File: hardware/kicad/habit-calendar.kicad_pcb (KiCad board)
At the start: 2 copper layers, 96 x 100 mm, 94 parts, among them J1 Conn_01x01, J10 Conn_01x01, J11 Conn_01x01, J12 Conn_01x01, J13 Conn_01x01, J14 Conn_01x01, J15 Conn_01x01, J16 Conn_01x01, J17 Conn_01x01, J18 Conn_01x01, J19 Conn_01x01, J2 Conn_01x01, J20 Conn_01x01, J21 Conn_01x01, J22 Conn_01x01, J23 Conn_01x01, J24 Conn_01x01, J25 Conn_01x01, J26 Conn_01x01, J27 Conn_01x01, J29 Conn_01x01, J30 Conn_01x01, J31 Conn_01x01, J4 Conn_01x10, J5 Conn_01x10, J6 Conn_01x01, J7 Conn_01x01, J8 Conn_01x01, J9 Conn_01x01, SW1 TS-1187A-B-A-B, SW10 TS-1187A-B-A-B, SW11 TS-1187A-B-A-B, SW12 TS-1187A-B-A-B, SW2 TS-1187A-B-A-B, SW3 TS-1187A-B-A-B, SW4 TS-1187A-B-A-B, SW5 TS-1187A-B-A-B, SW6 TS-1187A-B-A-B, SW7 TS-1187A-B-A-B, SW8 TS-1187A-B-A-B, SW9 TS-1187A-B-A-B, U1 PY32F002AF15P6TU

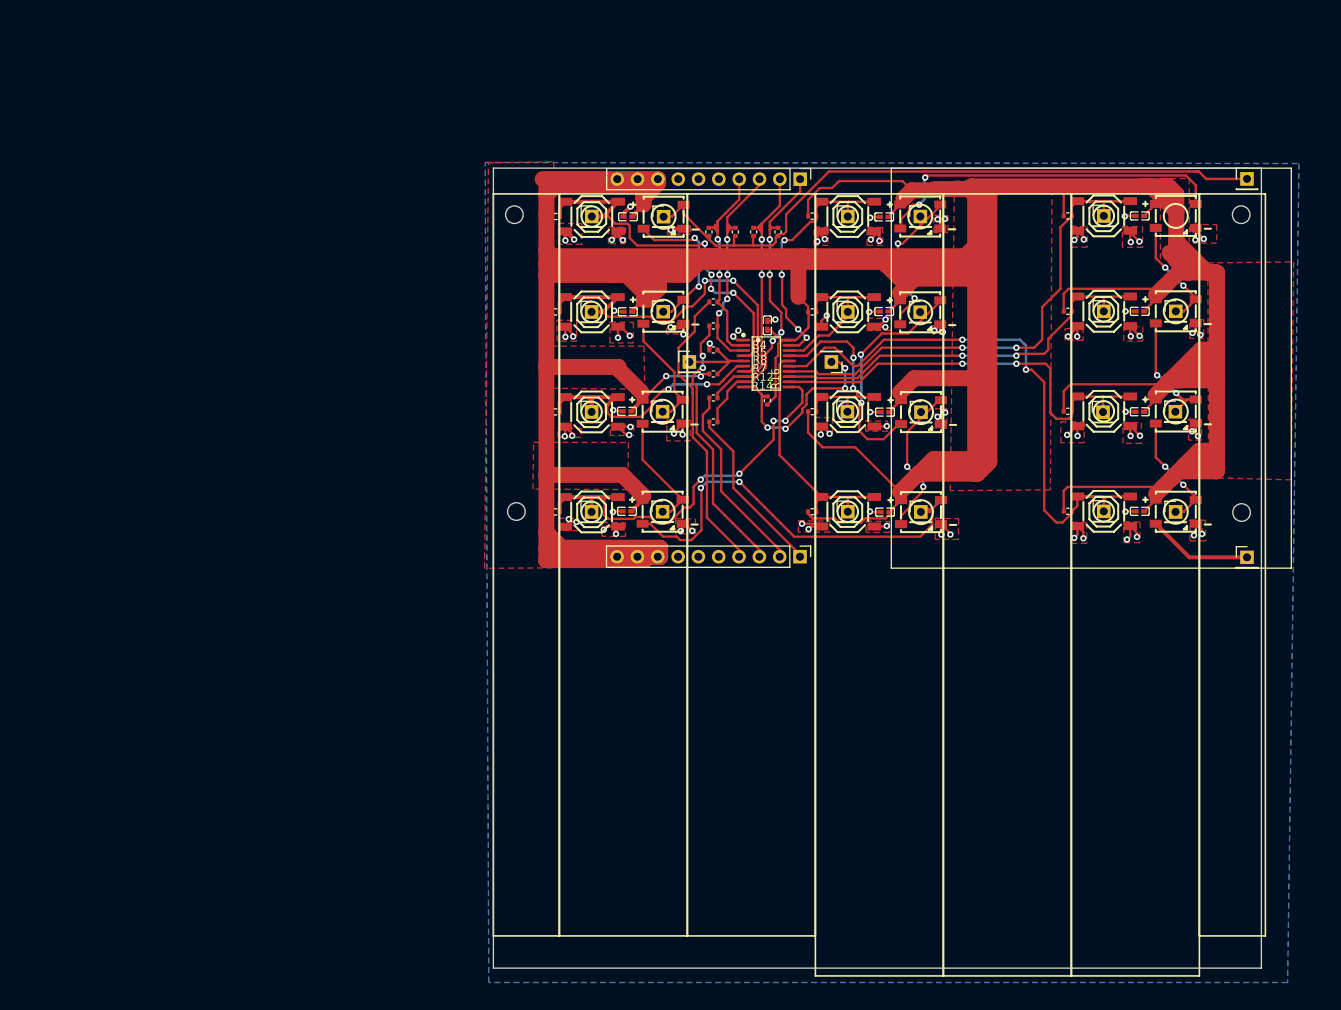
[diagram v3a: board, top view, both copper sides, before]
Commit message: Moved to a new heirarchical sheet. Instantiated two. Some PCB tweeks. Added Logo. Now going to use the replicate plugin to make another copy.
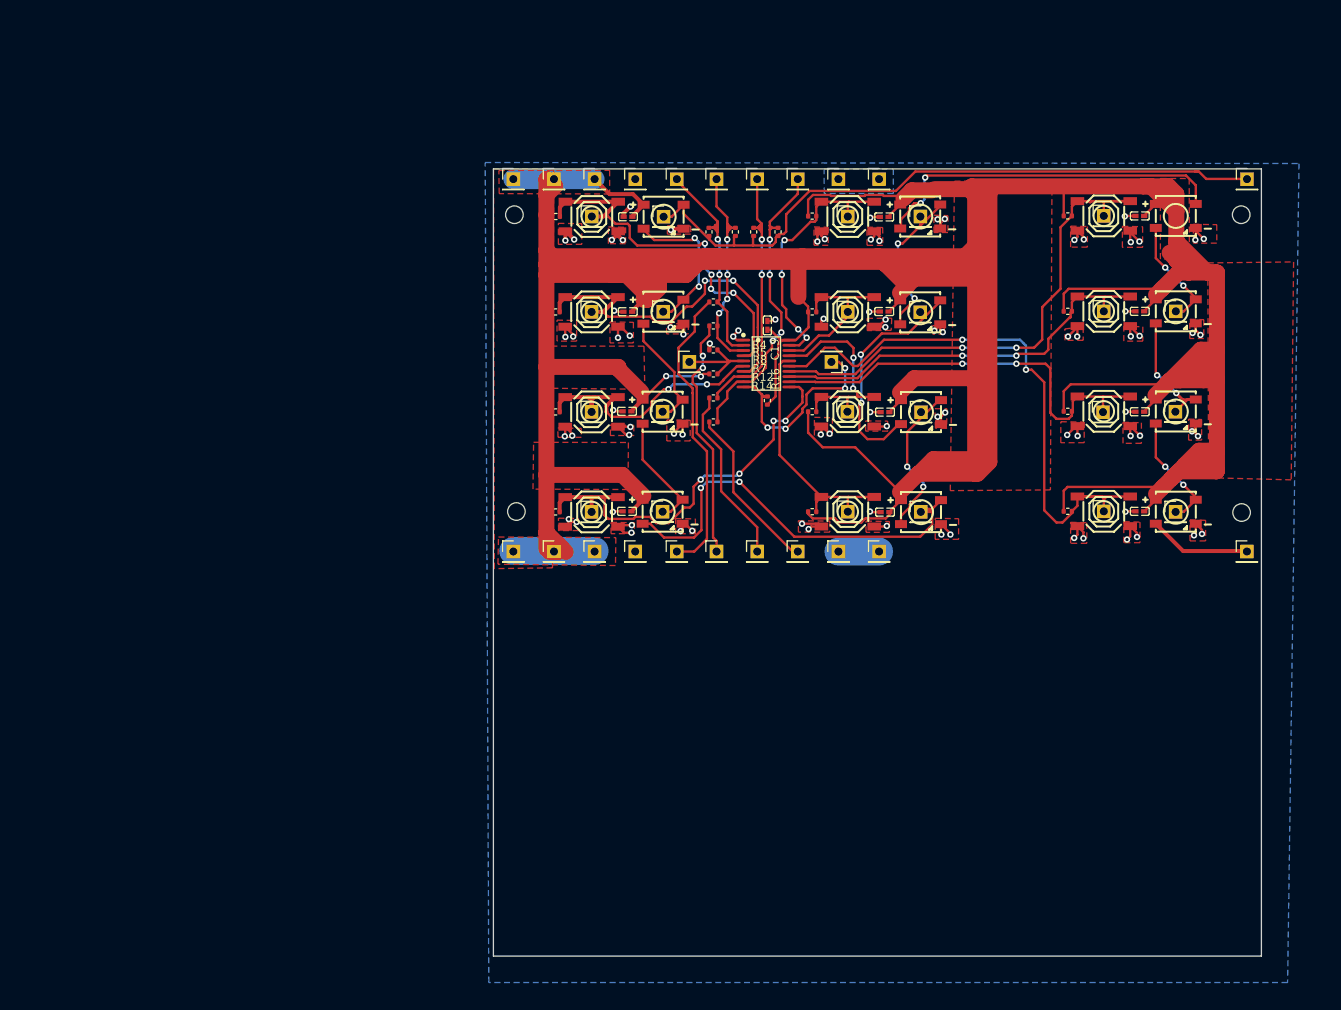
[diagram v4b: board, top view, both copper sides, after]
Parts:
- added G***: LOGO, LOGO, B.Cu at (197.8, 45.7)
- added J51: Conn_01x01, Connector_PinHeader_2.54mm:PinHeader_1x01_P2.54mm_Vertical, F.Cu at (125.2, 40.9)
- added J60: Conn_01x01, Connector_PinHeader_2.54mm:PinHeader_1x01_P2.54mm_Vertical, F.Cu at (130.2, 40.9)
- added J63: Conn_01x01, Connector_PinHeader_2.54mm:PinHeader_1x01_P2.54mm_Vertical, F.Cu at (160.7, 40.9)
- added J64: Conn_01x01, Connector_PinHeader_2.54mm:PinHeader_1x01_P2.54mm_Vertical, F.Cu at (155.6, 40.9)
- added J65: Conn_01x01, Connector_PinHeader_2.54mm:PinHeader_1x01_P2.54mm_Vertical, F.Cu at (135.4, 40.9)
- added J66: Conn_01x01, Connector_PinHeader_2.54mm:PinHeader_1x01_P2.54mm_Vertical, F.Cu at (140.4, 40.9)
- added J67: Conn_01x01, Connector_PinHeader_2.54mm:PinHeader_1x01_P2.54mm_Vertical, F.Cu at (145.5, 40.9)
- added J68: Conn_01x01, Connector_PinHeader_2.54mm:PinHeader_1x01_P2.54mm_Vertical, F.Cu at (150.6, 40.9)
- added J69: Conn_01x01, Connector_PinHeader_2.54mm:PinHeader_1x01_P2.54mm_Vertical, F.Cu at (115.0, 87.5)
- added J70: Conn_01x01, Connector_PinHeader_2.54mm:PinHeader_1x01_P2.54mm_Vertical, F.Cu at (120.1, 87.5)
- added J71: Conn_01x01, Connector_PinHeader_2.54mm:PinHeader_1x01_P2.54mm_Vertical, F.Cu at (125.2, 87.5)
- added J72: Conn_01x01, Connector_PinHeader_2.54mm:PinHeader_1x01_P2.54mm_Vertical, F.Cu at (130.2, 87.5)
- added J73: Conn_01x01, Connector_PinHeader_2.54mm:PinHeader_1x01_P2.54mm_Vertical, F.Cu at (155.6, 87.5)
- added J74: Conn_01x01, Connector_PinHeader_2.54mm:PinHeader_1x01_P2.54mm_Vertical, F.Cu at (160.7, 87.5)
- added J75: Conn_01x01, Connector_PinHeader_2.54mm:PinHeader_1x01_P2.54mm_Vertical, F.Cu at (135.4, 87.5)
- added J76: Conn_01x01, Connector_PinHeader_2.54mm:PinHeader_1x01_P2.54mm_Vertical, F.Cu at (140.4, 87.5)
- added J77: Conn_01x01, Connector_PinHeader_2.54mm:PinHeader_1x01_P2.54mm_Vertical, F.Cu at (145.5, 87.5)
- added J78: Conn_01x01, Connector_PinHeader_2.54mm:PinHeader_1x01_P2.54mm_Vertical, F.Cu at (150.6, 87.5)
- C1, C10, C11, C12, C13, C2, C3, C4, C5, C6, C7, C8, C9: footprint easyeda2kicadLocal:C0402 -> easyeda2kicad:C0402
- J4, J5: value Conn_01x10 -> Conn_01x01; footprint Connector_PinHeader_2.54mm:PinHeader_1x10_P2.54mm_Vertical -> Connector_PinHeader_2.54mm:PinHeader_1x01_P2.54mm_Vertical
- LED1, LED10, LED11, LED12, LED2, LED3, LED4, LED5, LED6, LED7, LED8, LED9: footprint easyeda2kicadLocal3:LED-SMD_4P-L5.0-W5.0-BL_XL-5050RGBC -> easyeda2kicad:LED-SMD_4P-L5.0-W5.0-BL_XL-5050RGBC
- moved J5 56.3 mm to (120.1, 40.9), turned to 0 degrees
- moved J4 35.9 mm to (115.0, 40.9), turned to 0 degrees
- moved J23 0.73 mm to (206.7, 87.5)
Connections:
- net /SW12 renamed /habit-calender-subsheet-for-replica/SW12
- net /SW6 renamed /habit-calender-subsheet-for-replica/SW6
- net /SW8 renamed /habit-calender-subsheet-for-replica/SW8
- net /SW9 renamed /habit-calender-subsheet-for-replica/SW9
- net /WS2812b - Din renamed /habit-calender-subsheet-for-replica/WS2812b - Din
- J4 pad 1: /PF1 -> +5V
- J5 pad 1: Net-(R14-Pad1) -> +5V
- R12 pad 1: Net-(R12-Pad1) -> /habit-calender-subsheet-for-replica1/PF0
- R12 pad 2: /PF0 -> /habit-calender-subsheet-for-replica/PF0
- R14 pad 1: Net-(R14-Pad1) -> /habit-calender-subsheet-for-replica1/PF1
- R14 pad 2: /PF1 -> /habit-calender-subsheet-for-replica/PF1
- R20 pad 2: /PA13 -> /habit-calender-subsheet-for-replica/PA13
- R21 pad 2: /PA14 -> /habit-calender-subsheet-for-replica/PA14
- R22 pad 2: /PF0 -> /habit-calender-subsheet-for-replica/PF0
- R23 pad 2: /PF1 -> /habit-calender-subsheet-for-replica/PF1
- R4 pad 1: Net-(R4-Pad1) -> /habit-calender-subsheet-for-replica1/PA13
- R4 pad 2: /PA13 -> /habit-calender-subsheet-for-replica/PA13
- R5 pad 1: Net-(R5-Pad1) -> /habit-calender-subsheet-for-replica1/PA14
- R5 pad 2: /PA14 -> /habit-calender-subsheet-for-replica/PA14
- U1 pad 2: /PA13 -> /habit-calender-subsheet-for-replica/PA13
- U1 pad 3: /PA14 -> /habit-calender-subsheet-for-replica/PA14
- U1 pad 8: /PF0 -> /habit-calender-subsheet-for-replica/PF0
- U1 pad 9: /PF1 -> /habit-calender-subsheet-for-replica/PF1
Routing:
- net +5V: track 708.2 -> 661.0 mm
- net /habit-calender-subsheet-for-replica/PF1: track 0.00 -> 38.3 mm, vias 0 -> 4
- net /PF1: track 38.3 -> 0.00 mm, vias 4 -> 0
- net /habit-calender-subsheet-for-replica1/PA13: track 0.00 -> 37.1 mm
- net Net-(R4-Pad1): track 36.1 -> 0.00 mm
- net /PF0: track 34.4 -> 0.00 mm, vias 2 -> 0
- net /habit-calender-subsheet-for-replica/PF0: track 0.00 -> 33.9 mm, vias 0 -> 2
- net Net-(R5-Pad1): track 33.0 -> 0.00 mm, vias 2 -> 0
- net /habit-calender-subsheet-for-replica1/PA14: track 0.00 -> 31.3 mm, vias 0 -> 2
- net /habit-calender-subsheet-for-replica/PA13: track 0.00 -> 28.5 mm, vias 0 -> 2
- net /PA14: track 28.2 -> 0.00 mm, vias 4 -> 0
- net /PA13: track 27.4 -> 0.00 mm, vias 2 -> 0
- net /habit-calender-subsheet-for-replica/PA14: track 0.00 -> 27.3 mm, vias 0 -> 4
- net Net-(R12-Pad1): track 23.7 -> 0.00 mm
- net /habit-calender-subsheet-for-replica1/PF0: track 0.00 -> 23.0 mm
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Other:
- board size 96 x 100 mm -> 96 x 98.4 mm
- board text added: "+5V"
- board text added: "Boot0 - PB6/PF4"
- board text added: "BradleyConn.space"
- board text added: "GND"
- board text added: "Habit Calendar Module Rev 0"
- board text added: "Inspired by Simone Giertz"
- board text added: "Led in"
- board text added: "Led out"
- board text added: "PA0"
- board text added: "PA1"
- board text added: "PA13"
- board text added: "PA14"
- board text added: "PA2"
- board text added: "PA3"
- board text added: "PA4"
- board text added: "PA5"
- board text added: "PA6"
- board text added: "PA7"
- board text added: "PB0"
- board text added: "PB1"
- board text added: "PB2"
- board text added: "PB3"
- board text added: "PF0"
- board text added: "PF1"
- board text added: "nRst - PF2"

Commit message: Sent to production!
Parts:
- removed J23, J69, J70, J71, J72, J73, J74: Conn_01x01, Connector_PinHeader_2.54mm:PinHeader_1x01_P2.54mm_Vertical
- added C14: 100nf, easyeda2kicad:C0402, F.Cu at (129.3, 94.8)
- added C15: 100nf, easyeda2kicad:C0402, F.Cu at (129.3, 106.6)
- added C16: 100nf, easyeda2kicad:C0402, F.Cu at (129.2, 119.1)
- added C17: 100nf, easyeda2kicad:C0402, F.Cu at (129.2, 131.6)
- added C18: 100nf, easyeda2kicad:C0402, F.Cu at (161.4, 94.8)
- added C19: 100nf, easyeda2kicad:C0402, F.Cu at (161.4, 106.6)
- added C20: 100nf, easyeda2kicad:C0402, F.Cu at (161.5, 119.2)
- added C21: 100nf, easyeda2kicad:C0402, F.Cu at (161.5, 131.7)
- added C22: 100nf, easyeda2kicad:C0402, F.Cu at (193.3, 94.7)
- added C23: 100nf, easyeda2kicad:C0402, F.Cu at (193.3, 106.6)
- added C24: 100nf, easyeda2kicad:C0402, F.Cu at (193.3, 119.1)
- added C25: 100nf, easyeda2kicad:C0402, F.Cu at (193.3, 131.6)
- added C26: 100nf, easyeda2kicad:C0402, F.Cu at (146.8, 108.3)
- added H5: MountingHole, MountingHole:MountingHole_2.2mm_M2, F.Cu at (115.1, 94.5)
- added H6: MountingHole, MountingHole:MountingHole_2.2mm_M2, F.Cu at (115.0, 131.6)
- added H7: MountingHole, MountingHole:MountingHole_2.2mm_M2, F.Cu at (206.0, 94.5)
- added H8: MountingHole, MountingHole:MountingHole_2.2mm_M2, F.Cu at (206.0, 131.7)
- added J32: Conn_01x01, Connector_PinHeader_2.54mm:PinHeader_1x01_P2.54mm_Vertical, F.Cu at (133.8, 94.8)
- added J33: Conn_01x01, Connector_PinHeader_2.54mm:PinHeader_1x01_P2.54mm_Vertical, F.Cu at (133.7, 106.6)
- added J34: Conn_01x01, Connector_PinHeader_2.54mm:PinHeader_1x01_P2.54mm_Vertical, F.Cu at (133.7, 119.1)
- added J35: Conn_01x01, Connector_PinHeader_2.54mm:PinHeader_1x01_P2.54mm_Vertical, F.Cu at (133.7, 131.6)
- added J36: Conn_01x01, Connector_PinHeader_2.54mm:PinHeader_1x01_P2.54mm_Vertical, F.Cu at (165.9, 94.7)
- added J37: Conn_01x01, Connector_PinHeader_2.54mm:PinHeader_1x01_P2.54mm_Vertical, F.Cu at (165.9, 106.7)
- added J38: Conn_01x01, Connector_PinHeader_2.54mm:PinHeader_1x01_P2.54mm_Vertical, F.Cu at (166.0, 119.2)
- added J40: Conn_01x01, Connector_PinHeader_2.54mm:PinHeader_1x01_P2.54mm_Vertical, F.Cu at (156.8, 94.7)
- added J41: Conn_01x01, Connector_PinHeader_2.54mm:PinHeader_1x01_P2.54mm_Vertical, F.Cu at (165.9, 131.7)
- added J43: Conn_01x01, Connector_PinHeader_2.54mm:PinHeader_1x01_P2.54mm_Vertical, F.Cu at (197.8, 106.6)
- added J44: Conn_01x01, Connector_PinHeader_2.54mm:PinHeader_1x01_P2.54mm_Vertical, F.Cu at (197.8, 119.1)
- added J45: Conn_01x01, Connector_PinHeader_2.54mm:PinHeader_1x01_P2.54mm_Vertical, F.Cu at (197.8, 131.7)
- added J46: Conn_01x01, Connector_PinHeader_2.54mm:PinHeader_1x01_P2.54mm_Vertical, F.Cu at (206.7, 136.6)
- added J47: Conn_01x01, Connector_PinHeader_2.54mm:PinHeader_1x01_P2.54mm_Vertical, F.Cu at (156.8, 106.7)
- added J49: Conn_01x01, Connector_PinHeader_2.54mm:PinHeader_1x01_P2.54mm_Vertical, F.Cu at (156.8, 119.1)
- added J50: Conn_01x01, Connector_PinHeader_2.54mm:PinHeader_1x01_P2.54mm_Vertical, F.Cu at (156.8, 131.6)
- added J52: Conn_01x01, Connector_PinHeader_2.54mm:PinHeader_1x01_P2.54mm_Vertical, F.Cu at (137.0, 112.9)
- added J53: Conn_01x01, Connector_PinHeader_2.54mm:PinHeader_1x01_P2.54mm_Vertical, F.Cu at (124.8, 106.7)
- added J54: Conn_01x01, Connector_PinHeader_2.54mm:PinHeader_1x01_P2.54mm_Vertical, F.Cu at (124.8, 94.7)
- added J55: Conn_01x01, Connector_PinHeader_2.54mm:PinHeader_1x01_P2.54mm_Vertical, F.Cu at (124.8, 131.7)
- added J56: Conn_01x01, Connector_PinHeader_2.54mm:PinHeader_1x01_P2.54mm_Vertical, F.Cu at (124.8, 119.2)
- added J57: Conn_01x01, Connector_PinHeader_2.54mm:PinHeader_1x01_P2.54mm_Vertical, F.Cu at (154.8, 112.9)
- added J58: Conn_01x01, Connector_PinHeader_2.54mm:PinHeader_1x01_P2.54mm_Vertical, F.Cu at (188.8, 94.7)
- added J59: Conn_01x01, Connector_PinHeader_2.54mm:PinHeader_1x01_P2.54mm_Vertical, F.Cu at (188.8, 106.6)
- added J61: Conn_01x01, Connector_PinHeader_2.54mm:PinHeader_1x01_P2.54mm_Vertical, F.Cu at (188.7, 119.2)
- added J62: Conn_01x01, Connector_PinHeader_2.54mm:PinHeader_1x01_P2.54mm_Vertical, F.Cu at (188.8, 131.6)
- added J89: Conn_01x01, Connector_PinHeader_2.54mm:PinHeader_1x01_P2.54mm_Vertical, F.Cu at (115.0, 136.6)
- added J90: Conn_01x01, Connector_PinHeader_2.54mm:PinHeader_1x01_P2.54mm_Vertical, F.Cu at (120.1, 136.6)
- added J91: Conn_01x01, Connector_PinHeader_2.54mm:PinHeader_1x01_P2.54mm_Vertical, F.Cu at (125.2, 136.6)
- added J92: Conn_01x01, Connector_PinHeader_2.54mm:PinHeader_1x01_P2.54mm_Vertical, F.Cu at (130.2, 136.6)
- added J93: Conn_01x01, Connector_PinHeader_2.54mm:PinHeader_1x01_P2.54mm_Vertical, F.Cu at (155.6, 136.6)
- added J94: Conn_01x01, Connector_PinHeader_2.54mm:PinHeader_1x01_P2.54mm_Vertical, F.Cu at (160.7, 136.6)
- added J95: Conn_01x01, Connector_PinHeader_2.54mm:PinHeader_1x01_P2.54mm_Vertical, F.Cu at (135.4, 136.6)
- added J96: Conn_01x01, Connector_PinHeader_2.54mm:PinHeader_1x01_P2.54mm_Vertical, F.Cu at (140.4, 136.6)
- added J97: Conn_01x01, Connector_PinHeader_2.54mm:PinHeader_1x01_P2.54mm_Vertical, F.Cu at (145.5, 136.6)
- added J98: Conn_01x01, Connector_PinHeader_2.54mm:PinHeader_1x01_P2.54mm_Vertical, F.Cu at (150.6, 136.6)
- added LED13: XL-5050RGBC-WS2812B, easyeda2kicad:LED-SMD_4P-L5.0-W5.0-BL_XL-5050RGBC, F.Cu at (133.8, 94.8)
- added LED14: XL-5050RGBC-WS2812B, easyeda2kicad:LED-SMD_4P-L5.0-W5.0-BL_XL-5050RGBC, F.Cu at (133.8, 106.6)
- added LED15: XL-5050RGBC-WS2812B, easyeda2kicad:LED-SMD_4P-L5.0-W5.0-BL_XL-5050RGBC, F.Cu at (133.7, 119.1)
- added LED16: XL-5050RGBC-WS2812B, easyeda2kicad:LED-SMD_4P-L5.0-W5.0-BL_XL-5050RGBC, F.Cu at (133.7, 131.6)
- added LED17: XL-5050RGBC-WS2812B, easyeda2kicad:LED-SMD_4P-L5.0-W5.0-BL_XL-5050RGBC, F.Cu at (165.9, 94.7)
- added LED18: XL-5050RGBC-WS2812B, easyeda2kicad:LED-SMD_4P-L5.0-W5.0-BL_XL-5050RGBC, F.Cu at (165.9, 106.7)
- added LED19: XL-5050RGBC-WS2812B, easyeda2kicad:LED-SMD_4P-L5.0-W5.0-BL_XL-5050RGBC, F.Cu at (166.0, 119.2)
- added LED20: XL-5050RGBC-WS2812B, easyeda2kicad:LED-SMD_4P-L5.0-W5.0-BL_XL-5050RGBC, F.Cu at (166.0, 131.7)
- added LED21: XL-5050RGBC-WS2812B, easyeda2kicad:LED-SMD_4P-L5.0-W5.0-BL_XL-5050RGBC, F.Cu at (197.8, 94.7)
- added LED22: XL-5050RGBC-WS2812B, easyeda2kicad:LED-SMD_4P-L5.0-W5.0-BL_XL-5050RGBC, F.Cu at (197.8, 106.6)
- added LED23: XL-5050RGBC-WS2812B, easyeda2kicad:LED-SMD_4P-L5.0-W5.0-BL_XL-5050RGBC, F.Cu at (197.8, 119.1)
- added LED24: XL-5050RGBC-WS2812B, easyeda2kicad:LED-SMD_4P-L5.0-W5.0-BL_XL-5050RGBC, F.Cu at (197.8, 131.6)
- added R24: 10k, Resistor_SMD:R_0402_1005Metric, F.Cu at (152.4, 94.7)
- added R25: 10k, Resistor_SMD:R_0402_1005Metric, F.Cu at (152.4, 106.7)
- added R26: 0 ohm, Resistor_SMD:R_0402_1005Metric, F.Cu at (139.4, 96.7)
- added R27: 0 ohm, Resistor_SMD:R_0402_1005Metric, F.Cu at (142.7, 96.7)
- added R28: 10k, Resistor_SMD:R_0402_1005Metric, F.Cu at (152.4, 119.1)
- added R29: 0 ohm, Resistor_SMD:R_0402_1005Metric, F.Cu at (145.0, 96.7)
- added R30: 0 ohm, Resistor_SMD:R_0402_1005Metric, F.Cu at (148.1, 96.7)
- added R31: 10k, Resistor_SMD:R_0402_1005Metric, F.Cu at (152.4, 131.6)
- added R32: DNP, Resistor_SMD:R_0402_1005Metric, F.Cu at (140.0, 114.4)
- added R33: 10k, Resistor_SMD:R_0402_1005Metric, F.Cu at (140.0, 111.4)
- added R34: 10k, Resistor_SMD:R_0402_1005Metric, F.Cu at (120.3, 94.7)
- added R35: 10k, Resistor_SMD:R_0402_1005Metric, F.Cu at (120.3, 106.7)
- added R36: 10k, Resistor_SMD:R_0402_1005Metric, F.Cu at (120.3, 119.2)
- added R37: 10k, Resistor_SMD:R_0402_1005Metric, F.Cu at (120.3, 131.7)
- added R38: 10k, Resistor_SMD:R_0402_1005Metric, F.Cu at (184.3, 94.7)
- added R39: 10k, Resistor_SMD:R_0402_1005Metric, F.Cu at (146.8, 117.7)
- added R40: 10k, Resistor_SMD:R_0402_1005Metric, F.Cu at (184.3, 106.6)
- added R41: 0 ohm, Resistor_SMD:R_0402_1005Metric, F.Cu at (140.0, 105.4)
- added R42: 0 ohm, Resistor_SMD:R_0402_1005Metric, F.Cu at (140.0, 108.4)
- added R43: 0 ohm, Resistor_SMD:R_0402_1005Metric, F.Cu at (140.0, 117.4)
- added R44: 0 ohm, Resistor_SMD:R_0402_1005Metric, F.Cu at (140.0, 120.4)
- added R45: 10k, Resistor_SMD:R_0402_1005Metric, F.Cu at (184.3, 119.1)
- added R46: 10k, Resistor_SMD:R_0402_1005Metric, F.Cu at (184.3, 131.6)
- added SW13: TS-1187A-B-A-B, easyeda2kicad:SW-SMD_4P-L5.1-W5.1-P3.70-LS6.5-TL-2, F.Cu at (156.8, 94.7)
- added SW14: TS-1187A-B-A-B, easyeda2kicad:SW-SMD_4P-L5.1-W5.1-P3.70-LS6.5-TL-2, F.Cu at (156.8, 106.7)
- added SW15: TS-1187A-B-A-B, easyeda2kicad:SW-SMD_4P-L5.1-W5.1-P3.70-LS6.5-TL-2, F.Cu at (156.8, 119.1)
- added SW16: TS-1187A-B-A-B, easyeda2kicad:SW-SMD_4P-L5.1-W5.1-P3.70-LS6.5-TL-2, F.Cu at (156.8, 131.6)
- added SW17: TS-1187A-B-A-B, easyeda2kicad:SW-SMD_4P-L5.1-W5.1-P3.70-LS6.5-TL-2, F.Cu at (124.8, 94.7)
- added SW18: TS-1187A-B-A-B, easyeda2kicad:SW-SMD_4P-L5.1-W5.1-P3.70-LS6.5-TL-2, F.Cu at (124.8, 106.7)
- added SW19: TS-1187A-B-A-B, easyeda2kicad:SW-SMD_4P-L5.1-W5.1-P3.70-LS6.5-TL-2, F.Cu at (124.8, 119.2)
- added SW20: TS-1187A-B-A-B, easyeda2kicad:SW-SMD_4P-L5.1-W5.1-P3.70-LS6.5-TL-2, F.Cu at (124.8, 131.7)
- added SW21: TS-1187A-B-A-B, easyeda2kicad:SW-SMD_4P-L5.1-W5.1-P3.70-LS6.5-TL-2, F.Cu at (188.8, 94.7)
- added SW22: TS-1187A-B-A-B, easyeda2kicad:SW-SMD_4P-L5.1-W5.1-P3.70-LS6.5-TL-2, F.Cu at (188.8, 106.6)
- added SW23: TS-1187A-B-A-B, easyeda2kicad:SW-SMD_4P-L5.1-W5.1-P3.70-LS6.5-TL-2, F.Cu at (188.8, 119.1)
- added SW24: TS-1187A-B-A-B, easyeda2kicad:SW-SMD_4P-L5.1-W5.1-P3.70-LS6.5-TL-2, F.Cu at (188.8, 131.6)
- added U2: PY32F002AF15P6TU, easyeda2kicad:TSSOP-20_L6.5-W4.4-P0.65-LS6.4-BL, F.Cu at (146.6, 113.1)
- moved J75 1.17 mm to (135.5, 88.6)
- moved J77 1.17 mm to (145.5, 88.6)
- moved J78 1.17 mm to (150.6, 88.6)
- moved J76 1.17 mm to (140.4, 88.6)
- moved H2 0.34 mm to (115.0, 82.5)
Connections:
- LED12 pad 2: Net-(J23-Pad1) -> /habit-calender-subsheet-for-replica1/WS2812b - Din
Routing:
- net +5V: track 661.0 -> 1309.7 mm, vias 2 -> 4
- net GND: track 127.8 -> 244.9 mm, vias 84 -> 168
- net /habit-calender-subsheet-for-replica1/WS2812b - Din: track 0.00 -> 77.0 mm
- net /habit-calender-subsheet-for-replica1/SW12: track 0.00 -> 73.9 mm, vias 0 -> 2
- net /habit-calender-subsheet-for-replica1/SW9: track 0.00 -> 66.6 mm, vias 0 -> 2
- net Net-(J61-Pad1): track 0.00 -> 53.8 mm, vias 0 -> 2
- net Net-(J41-Pad1): track 0.00 -> 53.7 mm, vias 0 -> 2
- net Net-(J59-Pad1): track 0.00 -> 50.6 mm, vias 0 -> 2
- net /habit-calender-subsheet-for-replica1/SW8: track 0.00 -> 50.6 mm, vias 0 -> 4
- net Net-(J54-Pad1): track 0.00 -> 47.3 mm, vias 0 -> 4
- net /habit-calender-subsheet-for-replica1/SW6: track 0.00 -> 46.4 mm, vias 0 -> 2
- net Net-(J42-Pad1): track 0.00 -> 44.9 mm, vias 0 -> 2
- net /habit-calender-subsheet-for-replica1/PF1: track 21.4 -> 61.7 mm, vias 0 -> 4
- net /habit-calender-subsheet-for-replica1/outPA13: track 0.00 -> 37.1 mm
- net /habit-calender-subsheet-for-replica1/PF0: track 23.0 -> 58.8 mm, vias 0 -> 2
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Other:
- board text added: "LED Din"
- board text added: "LED Dout"
- board text removed: "Led in"
- board text removed: "Led out"
